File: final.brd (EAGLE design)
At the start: 100 x 80 mm, 84 parts, among them IC2 MEGA8-AI, IC4 7805, Q2 32.768kHz, U2 DS1307

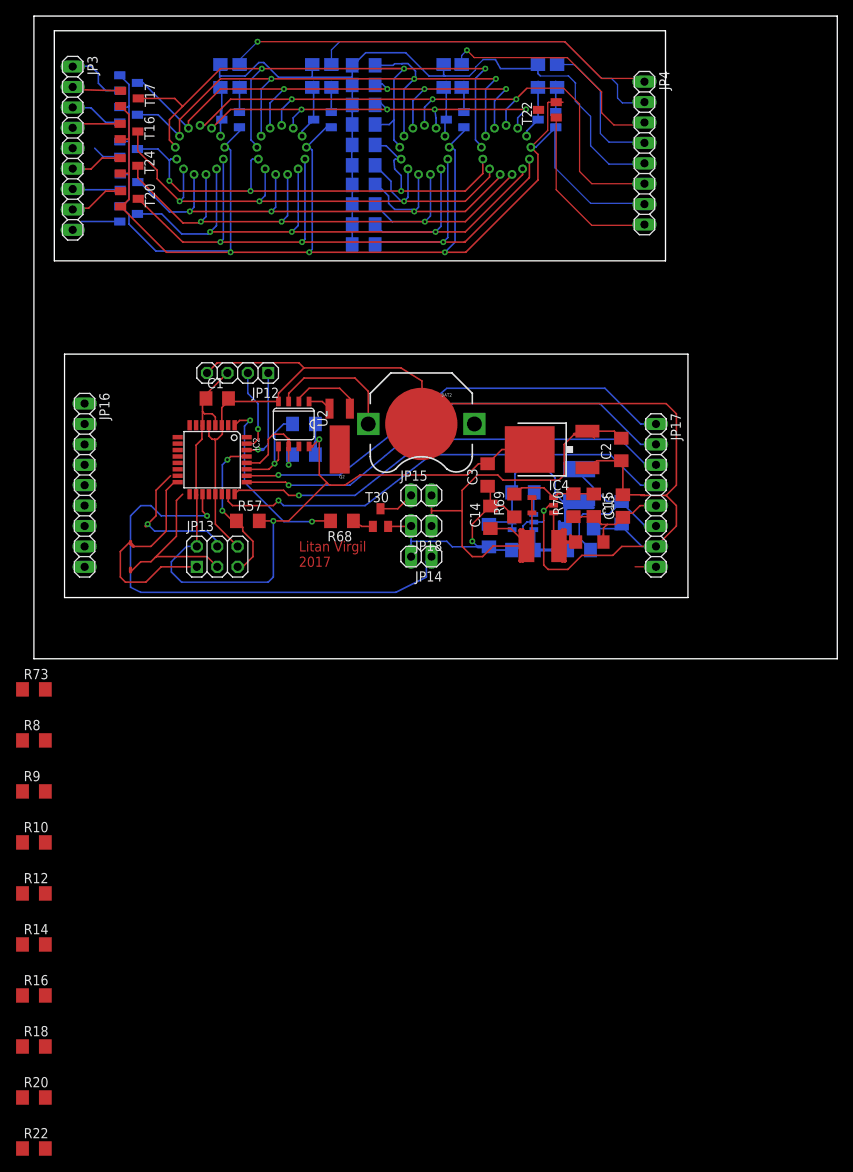
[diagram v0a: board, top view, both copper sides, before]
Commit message: added holes and milling
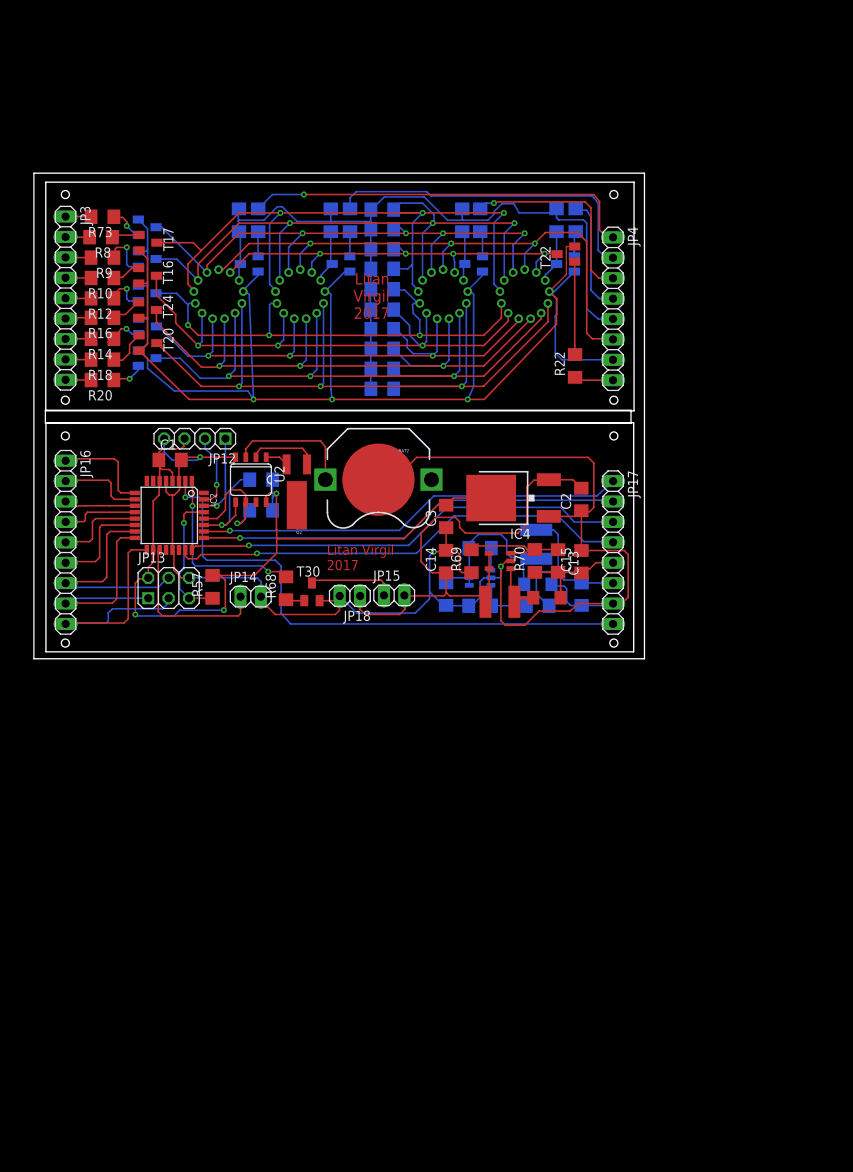
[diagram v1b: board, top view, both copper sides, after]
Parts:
- moved R22 118.4 mm to (67.4, 36.4), turned to 90 degrees
- moved R20 89.7 mm to (8.53, 34.7), turned to 180 degrees
- moved R18 85.9 mm to (8.53, 37.2), turned to 180 degrees
- moved R16 84.8 mm to (8.53, 42.4), turned to 180 degrees
- moved R14 75.9 mm to (8.53, 39.8), turned to 180 degrees
- moved R12 74.6 mm to (8.53, 44.9), turned to 180 degrees
- moved R10 70.8 mm to (8.53, 47.4), turned to 180 degrees
- moved R9 67.0 mm to (8.53, 49.9), turned to 180 degrees
- moved R8 63.2 mm to (8.36, 52.5), turned to 180 degrees
- moved R73 59.4 mm to (8.53, 55.0), turned to 180 degrees
- moved JP14 21.8 mm to (27.0, 7.73), turned to 0 degrees
- moved JP4 19.8 mm to (72.1, 43.6)
- moved JP3 18.7 mm to (3.94, 44.9)
- moved R1 18.1 mm to (43.4, 53.5)
- moved R3 18.1 mm to (43.4, 48.5)
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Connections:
- removed net N$11: IC2.17, JP16.9
- removed net N$12: IC2.16, JP16.8
- removed net N$13: IC2.15, JP16.7
- new net SELECT4.1: JP4.4, R36.2
- net MISO: now also IC2.16, JP16.8
- net MOSI: now also IC2.15, JP16.7
- net SCK: now also IC2.17, JP16.9; no longer JP4.4, R36.2
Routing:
- net N$37: track 2.61 -> 69.4 mm, vias 0 -> 1
- net BUTTON: track 62.6 -> 20.5 mm, vias 1 -> 0
- net GND: track 408.7 -> 391.3 mm, vias 5 -> 6
- net SELECT4.1: track 0.00 -> 14.7 mm
- net N$15: track 0.00 -> 12.7 mm
- net N$36: track 0.00 -> 12.5 mm
- net N$17: track 0.00 -> 11.1 mm
- net N$35: track 0.00 -> 10.5 mm
- net MOSI: track 17.7 -> 27.9 mm, vias 1 -> 0
- net N$38: track 21.7 -> 11.5 mm
- net N$19: track 0.00 -> 9.52 mm
- net N$21: track 0.00 -> 8.91 mm
- net N$96: track 8.40 -> 0.00 mm
- net N$97: track 8.40 -> 0.00 mm
- net SELECT3: track 86.6 -> 78.4 mm
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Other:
- board size 100 x 80 mm -> 76 x 60.4 mm

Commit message: adjusted footprint of inductors and diodes in a really nasty and non-ok way
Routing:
- net N$40: track 0.00 -> 3.56 mm
- net N$13: track 0.00 -> 3.56 mm
- net N$44: track 0.00 -> 3.38 mm
- net N$43: track 0.00 -> 3.38 mm
- net N$42: track 0.00 -> 1.42 mm
- net N$41: track 0.00 -> 1.42 mm
- net N$45: track 0.00 -> 1.24 mm
- net N$46: track 0.00 -> 0.89 mm
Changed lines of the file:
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@@
 <wire x1="3.7338" y1="34.4932" x2="3.9116" y2="34.671" width="0.2" layer="1"/>
+</signal>
+<signal name="N$13">
+<wire x1="55.4736" y1="8.89" x2="55.4736" y2="5.334" width="0.6096" layer="1"/>
+</signal>
+<signal name="N$40">
+<wire x1="60.452" y1="8.89" x2="60.452" y2="5.334" width="0.6096" layer="1"/>
+</signal>
+<signal name="N$41">
+<wire x1="61.341" y1="8.3566" x2="61.341" y2="6.9342" width="0.6096" layer="1"/>
+</signal>
+<signal name="N$42">
+<wire x1="66.3194" y1="8.3566" x2="66.3194" y2="6.9342" width="0.6096" layer="1"/>
+</signal>
+<signal name="N$43">
+<wire x1="60.8076" y1="11.7348" x2="64.1858" y2="11.7348" width="0.6096" layer="16"/>
+</signal>
+<signal name="N$44">
+<wire x1="60.8076" y1="16.891" x2="64.1858" y2="16.891" width="0.6096" layer="16"/>
+</signal>
+<signal name="N$45">
+<wire x1="60.2742" y1="9.9568" x2="60.2742" y2="8.7122" width="0.6096" layer="16"/>
+</signal>
+<signal name="N$46">
+<wire x1="65.2526" y1="9.6012" x2="65.2526" y2="8.7122" width="0.6096" layer="16"/>
 </signal>
 </signals>

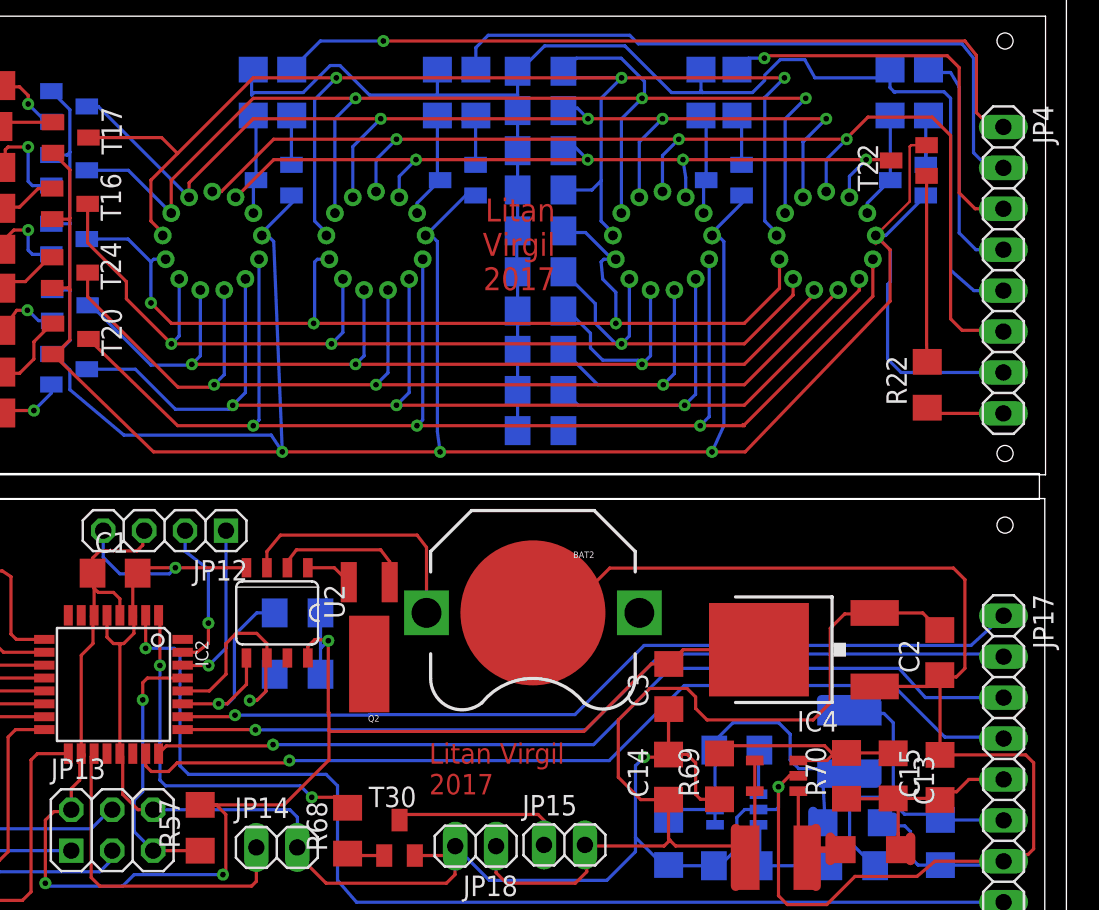
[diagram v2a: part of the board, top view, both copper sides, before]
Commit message: adjusted distance between vfds and moved name from top to tPlace layer
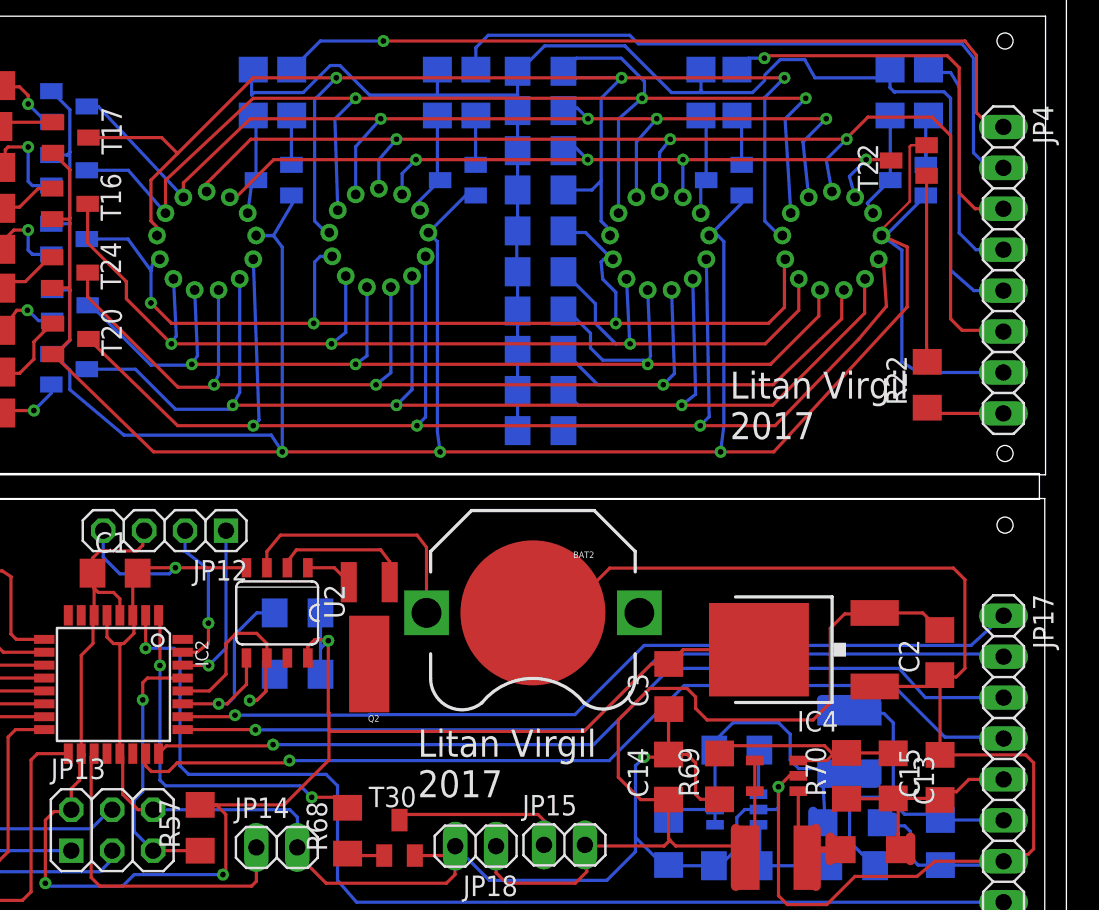
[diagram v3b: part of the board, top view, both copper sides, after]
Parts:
- moved U$1 0.36 mm to (22.6, 45.3)
- moved U$4 0.36 mm to (61.4, 45.3)
- moved U$2 0.25 mm to (33.3, 45.5)
- moved U$3 0.18 mm to (50.7, 45.3)
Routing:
- net GND: track 391.3 -> 393.0 mm
- net SEGMENT-H: track 70.0 -> 71.5 mm
- net SEGMENT-F: track 70.6 -> 72.1 mm
- net SEGMENT-A: track 78.7 -> 80.1 mm
- net SEGMENT-DP: track 97.1 -> 98.4 mm
- net SEGMENT-B: track 85.1 -> 86.3 mm
- net SEGMENT-Q: track 64.3 -> 65.2 mm
- net SEGMENT-E: track 89.4 -> 89.9 mm
- net N$22: track 6.26 -> 6.78 mm

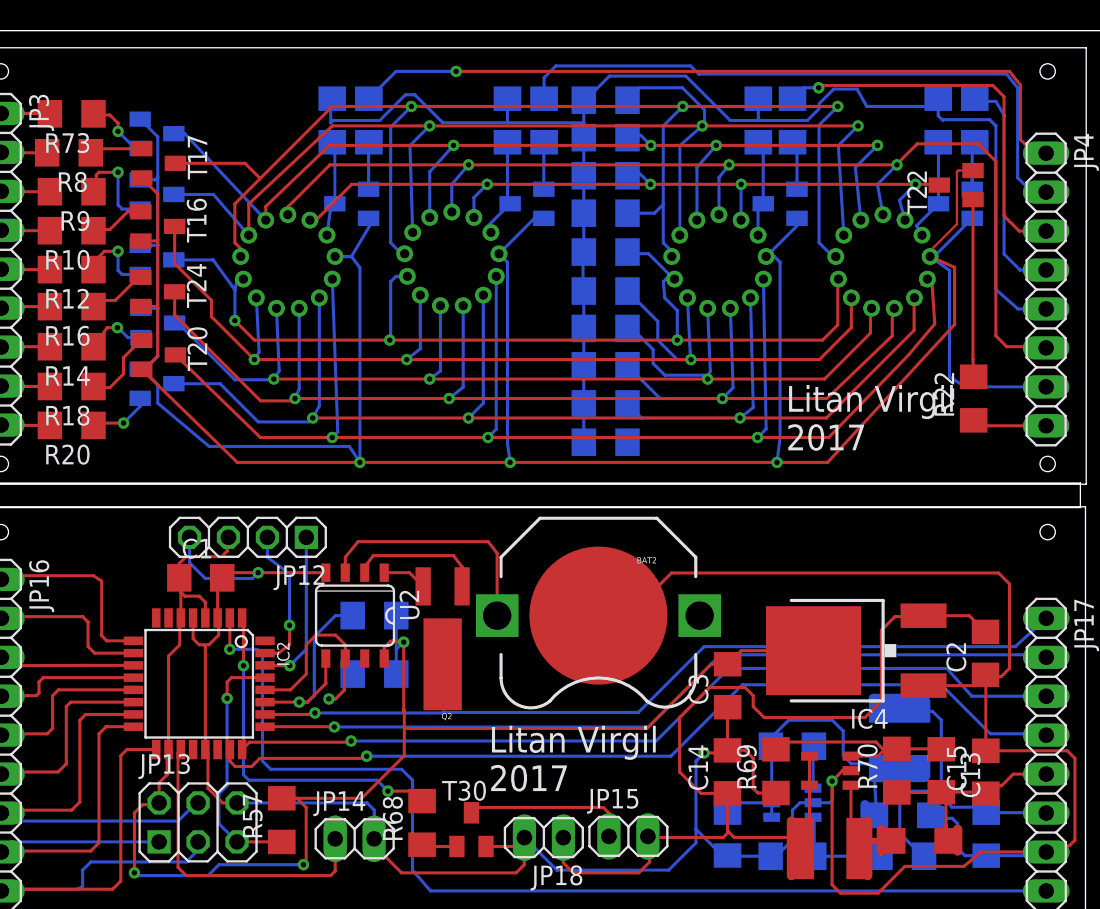
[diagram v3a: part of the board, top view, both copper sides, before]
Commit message: adjusted battery position and cleaned up the driver
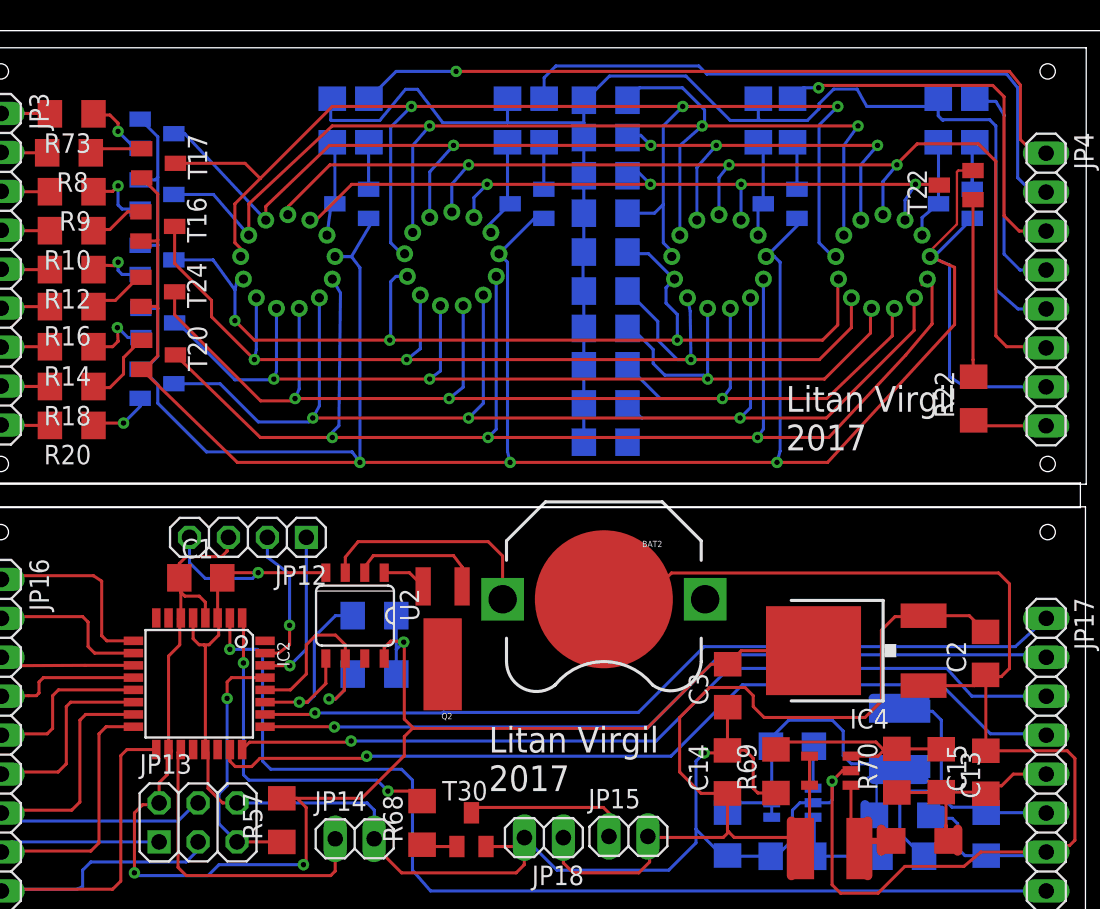
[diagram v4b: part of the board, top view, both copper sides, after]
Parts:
- moved BAT2 1.12 mm to (43.2, 23.4)
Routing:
- net N$47: track 0.00 -> 3.38 mm
- net N$43: track 3.38 -> 0.18 mm
- net N$28: track 6.64 -> 4.76 mm
- net N$93: track 20.1 -> 22.0 mm
- net N$30: track 5.17 -> 3.91 mm
- net N$71: track 15.8 -> 15.0 mm
